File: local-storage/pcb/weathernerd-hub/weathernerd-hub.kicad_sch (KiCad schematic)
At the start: 0 parts

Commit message: some schematic progress
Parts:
- added C1: 1nF, symbol Device:C
- added C2: 470nF, symbol Device:C
- added D1, D2: 1N4148, symbol Device:D
- added J1: WindNerd-Conn, symbol weathernerd:WindNerd-Conn
- added Q1: 2N7002, symbol Device:Q_NMOS
- added Q2: AO3401, symbol Device:Q_PMOS
- added R1, R2, R3: 10k, symbol Device:R
- added U1: ESP32-C6-SuperMini, symbol weathernerd:ESP32-C6-SuperMini
- added U2: MicroSD-SPI, symbol weathernerd:MicroSD-SPI
- added U3: BME280, symbol weathernerd:BME280
- added U4: DS3231, symbol weathernerd:DS3231
- added U5: OLED-Encoder-Btns, symbol weathernerd:OLED-Encoder-Btns
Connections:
- new net +3V3: J1.VCC, Q2.S, R3.2, U1.3V3, U2.3V3, U3.VCC, U4.VCC
- new net BAK_BTN: U1.23 (IO23), U5.BAK
- new net CON_BTN: U1.22 (IO22), U5.CON
- new net CPUMP: C1.1, D1.1 (K), D2.2 (A)
- new net ENC_A: U1.14 (IO14), U5.TRA
- new net ENC_B: U1.20 (IO20), U5.TRB
- new net ENC_PSH: U5.PSH
- new net GND: C1.2, C2.2, J1.GND, Q1.S, R2.2, U1.GND, U2.GND, U3.GND, U4.GND, U5.GND
- new net I2C_SCL: U1.7 (IO7), U3.SCL, U4.SCL, U5.SCL
- new net I2C_SDA: U1.6 (IO6), U3.SDA, U4.SDA, U5.SDA
- new net OLED_GATE: Q2.G, R3.1, U1.5 (IO5)
- new net OLED_PWR: Q2.D, U5.VCC
- new net PEAK: C2.1, D2.1 (K), Q1.D, R1.1
- new net PIEZO+: D1.2 (A)
- new net RAIN_ADC: R1.2, U1.0 (IO0)
- new net RAIN_RST: Q1.G, R2.1, U1.8 (IO8)
- new net SPI_CS: U1.3 (IO3), U2.CS
- new net SPI_MISO: U1.19 (IO19), U2.MISO
- new net SPI_MOSI: U1.18 (IO18), U2.MOSI
- new net SPI_SCK: U1.2 (IO2)
- new net WIND_TRIG: J1.TRG, U1.1 (IO1)
- new net WIND_TX: J1.RX, U1.4 (IO4)

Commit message: the start of a human touch
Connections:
- net GND: no longer C1.2
- net CPUMP: no longer names the net of C1.1, D1.1 (K), D2.2 (A)
- no-connect marks 0 -> 9
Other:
- moved on the sheet: C1, C2, D1, D2, J1, Q1, Q2, R1, R2, U1, U2, U3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

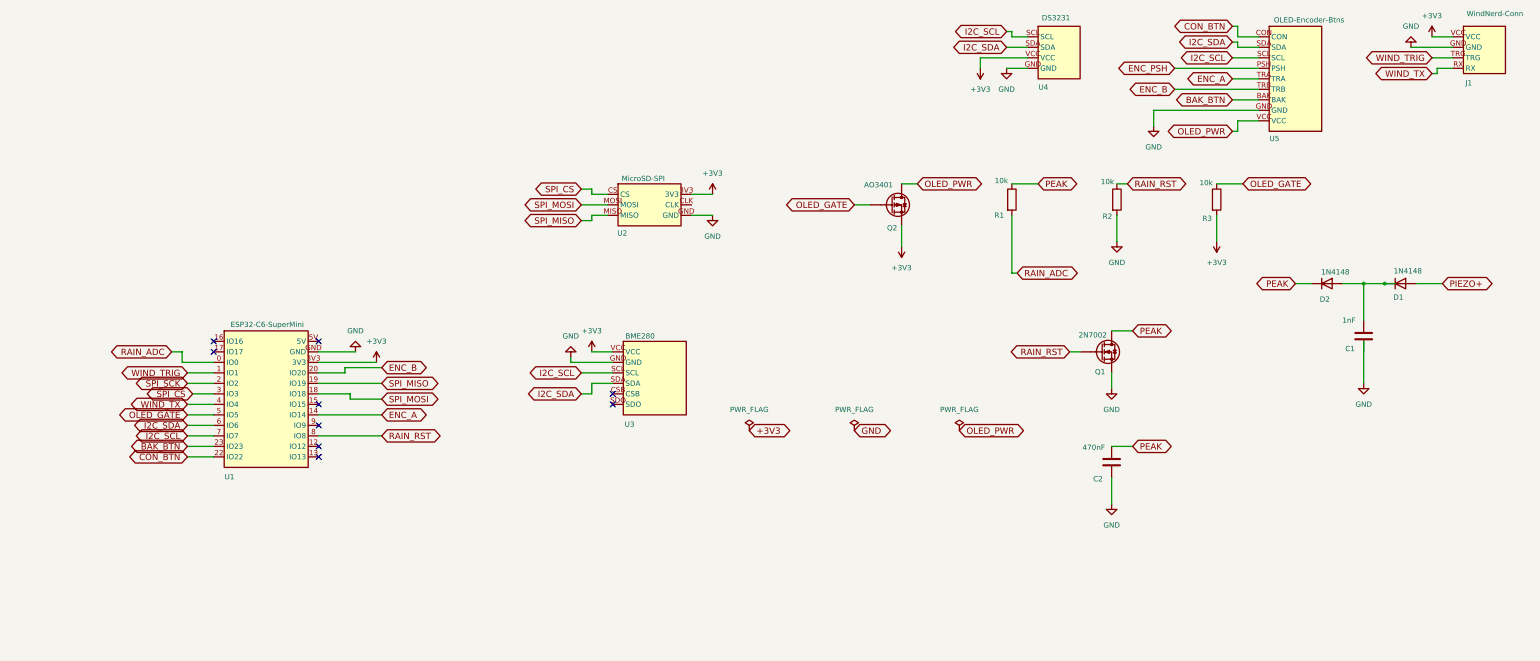
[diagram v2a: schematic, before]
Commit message: add MCP23008 and SIM7080G info
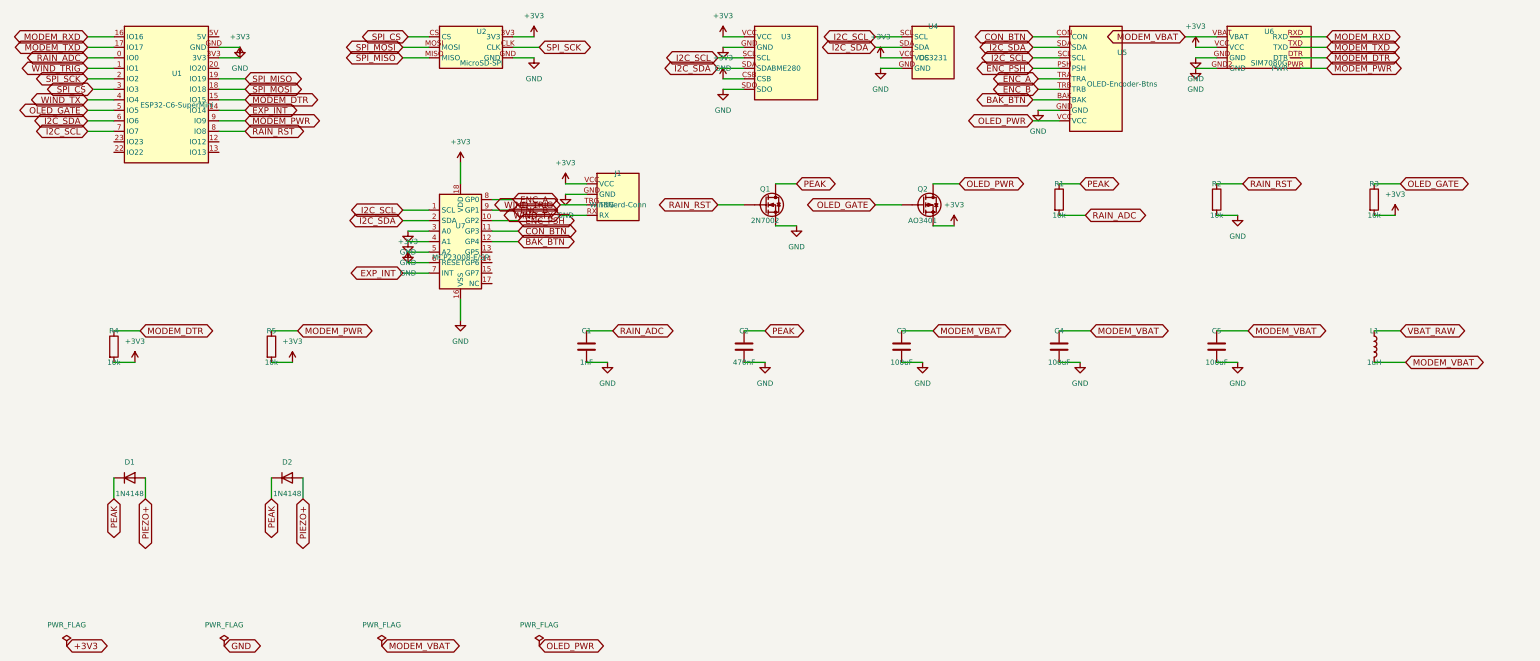
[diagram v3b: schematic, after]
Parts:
- added C3, C4, C5: 100uF, symbol Device:C
- added L1: 1uH, symbol Device:L
- added R4, R5: 10k, symbol Device:R
- added U6: SIM7080G, weathernerd:SIM7080G, symbol weathernerd:SIM7080G
- added U7: MCP23008-E/SP, Package_DIP:DIP-18_W7.62mm, symbol weathernerd:MCP23008
- J1: footprint (none) -> weathernerd:WindNerd-Conn
- U1: footprint (none) -> weathernerd:ESP32-C6-SuperMini
- U2: footprint (none) -> weathernerd:MicroSD-SPI
- U3: footprint (none) -> weathernerd:BME280
- U4: footprint (none) -> weathernerd:DS3231
- U5: footprint (none) -> weathernerd:OLED-Encoder-Btns
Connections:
- net +3V3: now also U3.CSB, R4.2, R5.2, U6.VCC, U7.18 (VDD), U7.6 (RESET)
- net BAK_BTN: now also U7.12 (GP4); no longer U1.23 (IO23)
- net CON_BTN: now also U7.11 (GP3); no longer U1.22 (IO22)
- net ENC_A: now also U7.8 (GP0); no longer U1.14 (IO14)
- net ENC_B: now also U7.9 (GP1); no longer U1.20 (IO20)
- net ENC_PSH: now also U7.10 (GP2)
- net GND: now also C1.2, U3.SDO, C3.2, C4.2, C5.2, U6.GND, U6.GND2 (GND), U7.16 (VSS), U7.3 (A0), U7.4 (A1), U7.5 (A2)
- net I2C_SCL: now also U7.1 (SCL)
- net I2C_SDA: now also U7.2 (SDA)
- net PEAK: now also D1.1 (K)
- net PIEZO+: now also D2.2 (A)
- net RAIN_ADC: now also C1.1
- net SPI_SCK: now also U2.CLK
- net MODEM_DTR: now reaches U1.15 (IO15)
- net MODEM_DTR: now also R4.1, U6.DTR
- net MODEM_RXD: now reaches U1.16 (IO16)
- net MODEM_RXD: now also U6.RXD
- net MODEM_TXD: now reaches U1.17 (IO17)
- net MODEM_TXD: now also U6.TXD
- net MODEM_PWR: now reaches U1.9 (IO9)
- net MODEM_PWR: now also R5.1, U6.PWR
- new net EXP_INT: U1.14 (IO14), U7.7 (INT)
- new net MODEM_VBAT: C3.1, C4.1, C5.1, L1.2, U6.VBAT
- new net VBAT_RAW: L1.1
- no-connect marks 9 -> 0
